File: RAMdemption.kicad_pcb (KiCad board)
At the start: 4 copper layers, 99 x 53.5 mm, 41 parts, among them J1 Conn_RAM_Expansion, U1 TC518512FTL-70, U10 TC518512FTL-70, U11 TC518512FTL-70, U12 TC518512FTL-70, U13 TC518512FTL-70, U14 TC518512FTL-70, U15 TC518512FTL-70, U16 TC518512FTL-70, U17 TC518512FTL-70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

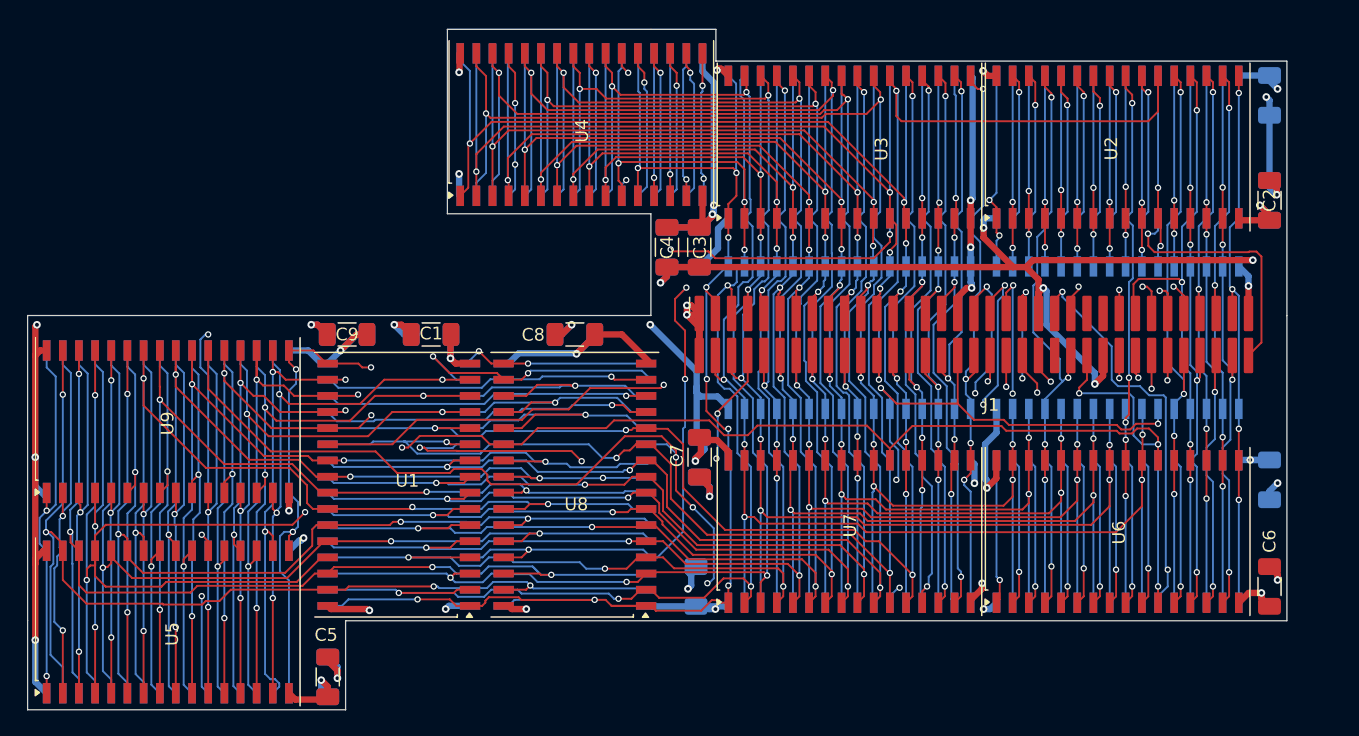
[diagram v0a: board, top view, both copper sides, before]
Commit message: redo cap placement
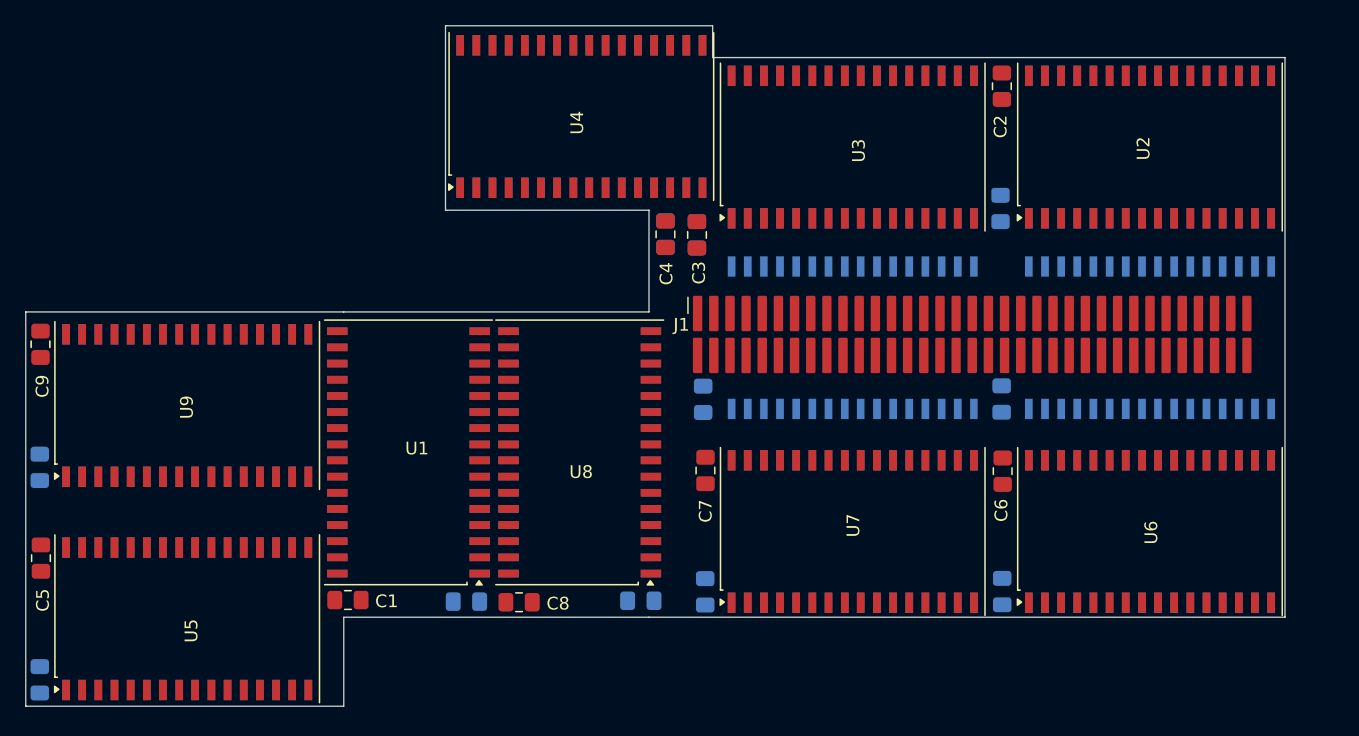
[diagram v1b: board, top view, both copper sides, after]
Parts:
- C1, C10, C11, C12, C13, C14, C15, C16, C17, C18, C19, C2, C20, C3, C4, C5, C6, C7, C8, C9: footprint Capacitor_SMD:C_1206_3216Metric_Pad1.33x1.80mm_HandSolder -> Capacitor_SMD:C_0805_2012Metric_Pad1.18x1.45mm_HandSolder
- moved C15 47.2 mm to (100.0, 62.9), turned to 90 degrees
- moved C19 46.3 mm to (99.5, 49.9), turned to -90 degrees
- moved C18 45.8 mm to (123.4, 47.9), turned to 90 degrees
- moved C14 33.9 mm to (123.4, 62.9), turned to 90 degrees
- moved C10 27.3 mm to (100.1, 78.0)
- moved C17 26.3 mm to (47.8, 68.2), turned to 90 degrees
- moved C5 24.4 mm to (47.9, 75.4)
- moved C9 24.1 mm to (47.9, 58.5), turned to -90 degrees
- moved C2 22.9 mm to (123.5, 38.3)
- moved C6 22.9 mm to (123.5, 68.5)
- moved C11 22.8 mm to (123.5, 78.0)
- moved C13 22.6 mm to (47.8, 84.9), turned to 90 degrees
- moved C1 21.9 mm to (72.1, 78.7)
- moved C16 21.5 mm to (81.4, 78.8), turned to 180 degrees
- moved C8 21.5 mm to (85.5, 78.8)
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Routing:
- net +5V: track 539.2 -> 0.00 mm, vias 28 -> 0
- net /RAM Bank 1/A18: track 274.8 -> 0.00 mm, vias 14 -> 0
- net /RAM Bank 1/A16: track 272.5 -> 0.00 mm, vias 12 -> 0
- net /RAM Bank 1/A15: track 266.8 -> 0.00 mm, vias 12 -> 0
- net /RAM Bank 1/A12: track 264.9 -> 0.00 mm, vias 12 -> 0
- net /RAM Bank 1/A17: track 261.2 -> 0.00 mm, vias 12 -> 0
- net /RAM Bank 1/A14: track 261.2 -> 0.00 mm, vias 12 -> 0
- net /RAM Bank 1/A6: track 260.6 -> 0.00 mm, vias 12 -> 0
- net /RAM Bank 1/A4: track 256.3 -> 0.00 mm, vias 12 -> 0
- net /RAM Bank 1/A7: track 256.2 -> 0.00 mm, vias 12 -> 0
- net /RAM Bank 1/A13: track 254.1 -> 0.00 mm, vias 12 -> 0
- net /RAM Bank 1/A9: track 253.5 -> 0.00 mm, vias 12 -> 0
- net /RAM Bank 1/A5: track 252.6 -> 0.00 mm, vias 12 -> 0
- net /RAM Bank 1/A3: track 250.9 -> 0.00 mm, vias 12 -> 0
- net /RAM Bank 1/A2: track 250.9 -> 0.00 mm, vias 12 -> 0
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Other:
- outline, holes or cut-outs redrawn

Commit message: six-layer stackup
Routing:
- added copper zone on In4.Cu, net GND
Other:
- copper layers 4 -> 6
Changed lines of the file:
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@@
 	(generator_version "9.0")
 	(general
-		(thickness 0.836)
+		(thickness 0.8244)
 		(legacy_teardrops no)
 	)
@@
 		(4 "In1.Cu" signal)
 		(6 "In2.Cu" signal)
+		(8 "In3.Cu" signal)
+		(10 "In4.Cu" signal)
 		(2 "B.Cu" signal)
 		(9 "F.Adhes" user "F.Adhesive")
@@
 				(type "Top Silk Screen")
 				(color "White")
-				(material "Peters SD2692")
+				(material "Liquid Photo")
 			)
 			(layer "F.Paste"
@@
 				(type "Top Solder Mask")
 				(color "Green")
-				(thickness 0.025)
-				(material "Elpemer AS 2467 SM-DG")
-				(epsilon_r 3.7)
+				(thickness 0.01)
+				(material "Liquid Ink")
+				(epsilon_r 3.3)
 				(loss_tangent 0)
 			)
 			(layer "F.Cu"
 				(type "copper")
-				(thickness 0.04)
+				(thickness 0.035)
 			)
 			(layer "dielectric 1"
 				(type "prepreg")
-				(color "FR4 natural")
-				(thickness 0.138)
-				(material "Pansonic R-1551(W)")
-				(epsilon_r 4.3)
+				(thickness 0.0764)
+				(material "1080")
+				(epsilon_r 3.91)
 				(loss_tangent 0)
 			)
 			(layer "In1.Cu"
 				(type "copper")
-				(thickness 0.035)
+				(thickness 0.0152)
 			)
 			(layer "dielectric 2"
 				(type "core")
 				(color "FR4 natural")
-				(thickness 0.36)
-				(material "Panasonic R-1566(W)")
+				(thickness 0.075)
+				(material "FR4")
 				(epsilon_r 4.6)
-				(loss_tangent 0)
+				(loss_tangent 0.02)
 			)
 			(layer "In2.Cu"
 				(type "copper")
-				(thickness 0.035)
+				(thickness 0.0152)
 			)
 			(layer "dielectric 3"
 				(type "prepreg")
+				(thickness 0.0764)
+				(material "1080")
+				(epsilon_r 3.91)
+				(loss_tangent 0) addsublayer
+				(thickness 0.218)
+				(material "7628")
+				(epsilon_r 4.4)
+				(loss_tangent 0) addsublayer
+				(thickness 0.0764)
+				(material "1080")
+				(epsilon_r 3.91)
+				(loss_tangent 0)
+			)
+			(layer "In3.Cu"
+				(type "copper")
+				(thickness 0.0152)
+			)
+			(layer "dielectric 4"
+				(type "core")
 				(color "FR4 natural")
-				(thickness 0.138)
-				(material "Pansonic R-1551(W)")
-				(epsilon_r 4.3)
+				(thickness 0.075)
+				(material "FR4")
+				(epsilon_r 4.6)
+				(loss_tangent 0.02)
+			)
+			(layer "In4.Cu"
+				(type "copper")
+				(thickness 0.0152)
+			)
+			(layer "dielectric 5"
+				(type "prepreg")
+				(thickness 0.0764)
+				(material "1080")
+				(epsilon_r 3.91)
 				(loss_tangent 0)
 			)
 			(layer "B.Cu"
 				(type "copper")
-				(thickness 0.04)
+				(thickness 0.035)
 			)
 			(layer "B.Mask"
 				(type "Bottom Solder Mask")
 				(color "Green")
-				(thickness 0.025)
-				(material "Elpemer AS 2467 SM-DG")
-				(epsilon_r 3.7)
+				(thickness 0.01)
+				(material "Liquid Ink")
+				(epsilon_r 3.3)
 				(loss_tangent 0)
 			)
@@
 				(type "Bottom Silk Screen")
 				(color "White")
-				(material "Peters SD2692")
+				(material "Liquid Photo")
 			)
 			(copper_finish "ENIG")
@@
 		(net 1)
 		(net_name "GND")
-		(layer "In1.Cu")
+		(layers "In1.Cu" "In4.Cu")
 		(hatch edge 0.5)
 		(connect_pads

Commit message: mostly rework
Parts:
- moved C7 3.57 mm to (99.9, 64.9), turned to 90 degrees
- moved C2 0.38 mm to (123.1, 38.3)
- moved C10 0.25 mm to (99.9, 78.0)
- moved C18 0.25 mm to (123.1, 47.9)
- moved C14 0.25 mm to (123.2, 62.9)
- moved U1 0.25 mm to (76.6, 67.1)
- moved U10 0.25 mm to (134.9, 73.3)
- moved U14 0.25 mm to (134.9, 58.0)
- moved U16 0.25 mm to (76.6, 67.1)
- moved U18 0.25 mm to (134.9, 43.0)
- moved U2 0.25 mm to (134.9, 43.0)
- moved U6 0.25 mm to (134.9, 73.3)
- moved C6 0.24 mm to (123.3, 68.4)
- moved C5 0.13 mm to (47.8, 75.4)
- moved C9 0.13 mm to (47.8, 58.5)
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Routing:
- net +5V: track 0.00 -> 422.1 mm, vias 0 -> 19
- net /RAM Bank 1/A15: track 0.00 -> 282.9 mm, vias 0 -> 11
- net /RAM Bank 1/A18: track 0.00 -> 282.2 mm, vias 0 -> 16
- net /RAM Bank 1/A16: track 0.00 -> 279.0 mm, vias 0 -> 15
- net /RAM Bank 1/A17: track 0.00 -> 276.4 mm, vias 0 -> 11
- net /RAM Bank 1/A14: track 0.00 -> 275.1 mm, vias 0 -> 12
- net /RAM Bank 1/A12: track 0.00 -> 272.6 mm, vias 0 -> 12
- net /RAM Bank 1/A7: track 0.00 -> 271.7 mm, vias 0 -> 12
- net /RAM Bank 1/A6: track 0.00 -> 268.5 mm, vias 0 -> 12
- net /RAM Bank 1/A5: track 0.00 -> 268.0 mm, vias 0 -> 12
- net /RAM Bank 1/A13: track 0.00 -> 267.2 mm, vias 0 -> 11
- net /RAM Bank 1/A8: track 0.00 -> 265.0 mm, vias 0 -> 11
- net /RAM Bank 1/A3: track 0.00 -> 264.6 mm, vias 0 -> 12
- net /RAM Bank 1/A4: track 0.00 -> 264.6 mm, vias 0 -> 12
- net /RAM Bank 1/A9: track 0.00 -> 261.5 mm, vias 0 -> 11
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
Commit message: finish
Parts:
- moved C14 5.51 mm to (123.3, 68.4), turned to -90 degrees
- moved C12 3.56 mm to (91.5, 78.8)
- moved C19 1.42 mm to (100.1, 51.2)
- moved C20 1.42 mm to (97.6, 51.2)
- moved C4 1.42 mm to (97.6, 51.2)
- moved C3 1.42 mm to (100.1, 51.2)
- moved C13 1.02 mm to (47.8, 83.9)
- moved C10 0.13 mm to (99.8, 78.0)
- moved C2 0.05 mm to (123.1, 38.2)
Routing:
- net +5V: track 422.1 -> 71.4 mm
- net ~{CS3}: track 0.00 -> 142.2 mm, vias 0 -> 2
- net ~{CS6}: track 13.2 -> 139.5 mm, vias 2 -> 6
- net ~{CS2}: track 0.00 -> 124.7 mm, vias 0 -> 5
- net /~{WE3}: track 28.8 -> 149.7 mm, vias 2 -> 7
- net /RAM Bank 1/D27: track 0.00 -> 117.7 mm, vias 0 -> 5
- net ~{CS5}: track 0.00 -> 105.0 mm, vias 0 -> 5
- net /RAM Bank 1/D30: track 28.2 -> 132.9 mm, vias 2 -> 3
- net /RAM Bank 1/D28: track 28.6 -> 128.6 mm, vias 2 -> 4
- net /RAM Bank 1/D26: track 27.6 -> 126.9 mm, vias 2 -> 3
- net /RAM Bank 1/D31: track 37.3 -> 133.8 mm, vias 2 -> 4
- net /RAM Bank 1/D24: track 31.3 -> 122.7 mm, vias 3 -> 5
- net /RAM Bank 1/D25: track 36.9 -> 127.1 mm, vias 2 -> 3
- net /RAM Bank 1/D29: track 37.4 -> 126.4 mm, vias 2 -> 4
- net /RAM Bank 1/D7: track 36.2 -> 108.0 mm, vias 2 -> 5
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- added copper zone on In2.Cu, net +5V

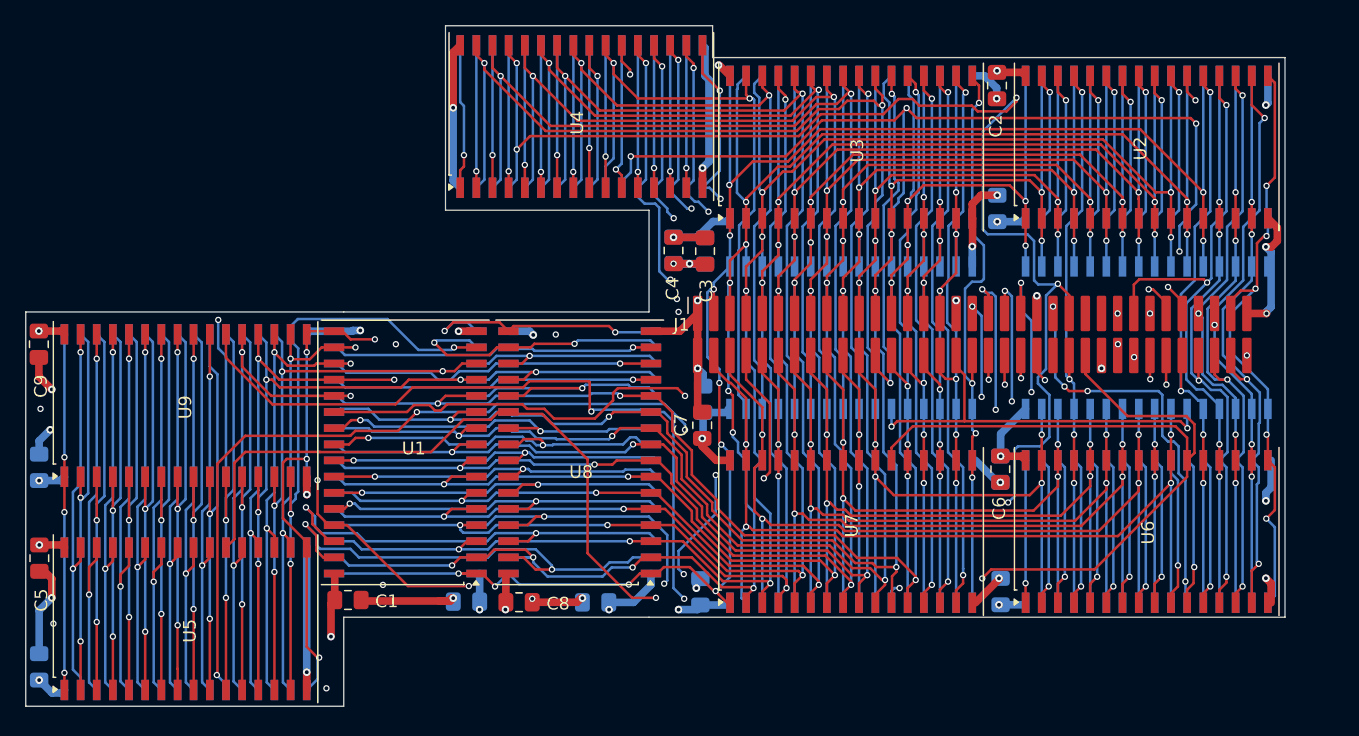
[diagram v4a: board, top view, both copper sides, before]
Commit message: add board name, 3d connector model
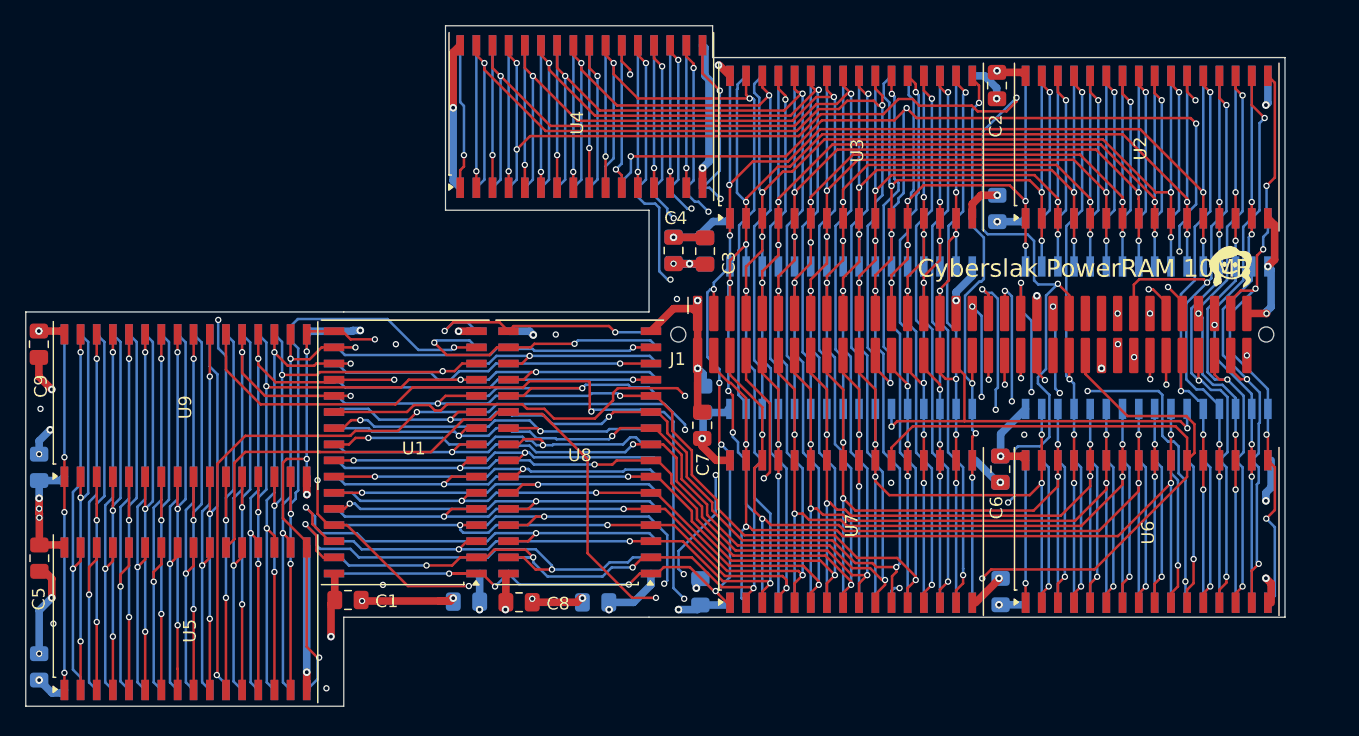
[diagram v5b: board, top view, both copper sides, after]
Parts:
- added G***: LOGO, RAMdemption:Me, F.Cu at (141.4, 52.5)
- J1: footprint RAMdemption:TE_5-104652-7_NoHoles -> RAMdemption:TE_5-104652-7
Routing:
- net +5V: track 71.4 -> 76.5 mm, vias 19 -> 20
- net /RAM Bank 1/A16: track 279.2 -> 276.8 mm
- net ~{CS4}: track 130.1 -> 131.3 mm
- net GND: track 111.2 -> 110.6 mm, vias 36 -> 39
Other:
- board text added: "Cyberslak PowerRAM 10MB"
